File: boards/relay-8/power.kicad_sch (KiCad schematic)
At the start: 7 parts, among them U3 LM317_SOT-223

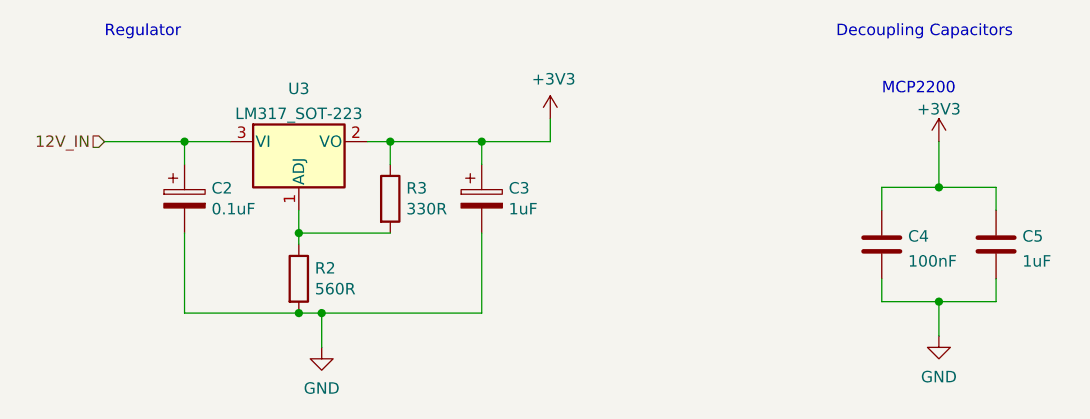
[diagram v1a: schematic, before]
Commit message: Added 12V for regulator
Signed-off-by: Computroniks <mnickson@sidingsmedia.com>
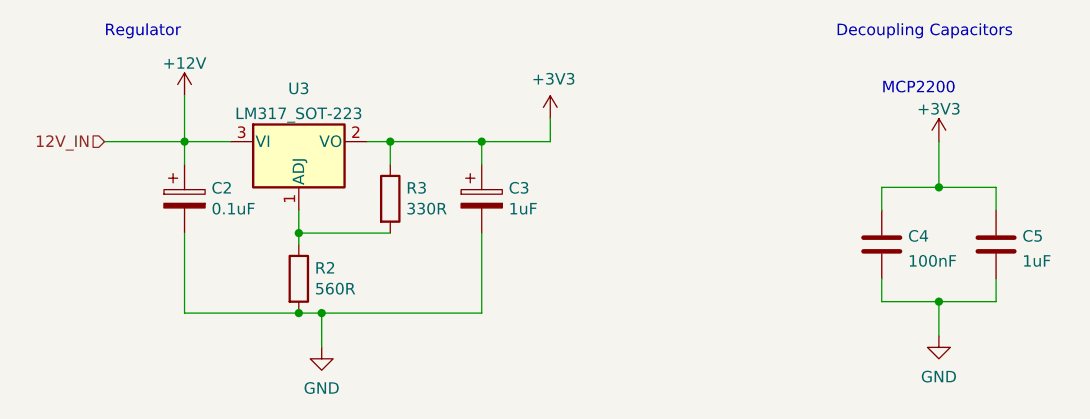
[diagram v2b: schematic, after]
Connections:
- net 12V_IN renamed +12V
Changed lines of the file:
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@@
+    (stroke (width 0) (type default) (color 0 0 0 0))
+  )
+  (wire (pts (xy 59.69 26.67) (xy 59.69 31.75))
     (stroke (width 0) (type default) (color 0 0 0 0))
   )
@@
     (pin "2")
   )
+  (symbol (lib_id "power:+12V") (at 59.69 26.67 0) (unit 1)
+    (in_bom yes) (on_board yes) (fields_autoplaced)
+    (property "Reference" "#PWR?" (id 0) (at 59.69 30.48 0)
+      (effects (font (size 1.27 1.27)) hide)
+    )
+    (property "Value" "+12V" (id 1) (at 59.69 23.0655 0))
+    (property "Footprint" "" (id 2) (at 59.69 26.67 0)
+      (effects (font (size 1.27 1.27)) hide)
+    )
+    (property "Datasheet" "" (id 3) (at 59.69 26.67 0)
+      (effects (font (size 1.27 1.27)) hide)
+    )
+    (pin "1")
+  )
   (symbol (lib_id "power:GND") (at 143.51 53.34 0) (unit 1)
